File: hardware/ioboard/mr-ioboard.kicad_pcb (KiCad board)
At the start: 4 copper layers, 65 x 80 mm, 126 parts, among them J1 Conn_01x40_Shielded, J2 USB_C_Receptacle_USB2.0, J3 Conn_01x06, J4 Micro_SD_Card_Det, J5 Conn_01x04, J6 Conn_01x02, Q1 2N7002, SW1 SW_Push, U1 TPS62822, U10 F1C200S, U11 TPS54202DDC, U2 TPS56637, U3 TPD2E2U06, U4 DS90C363, U5 TPD2E2U06, U6 LD3985M28R_SOT23, U7 TPS62822, U8 FUSB302BMPX, U9 TPD2E2U06, Y1 24MHz

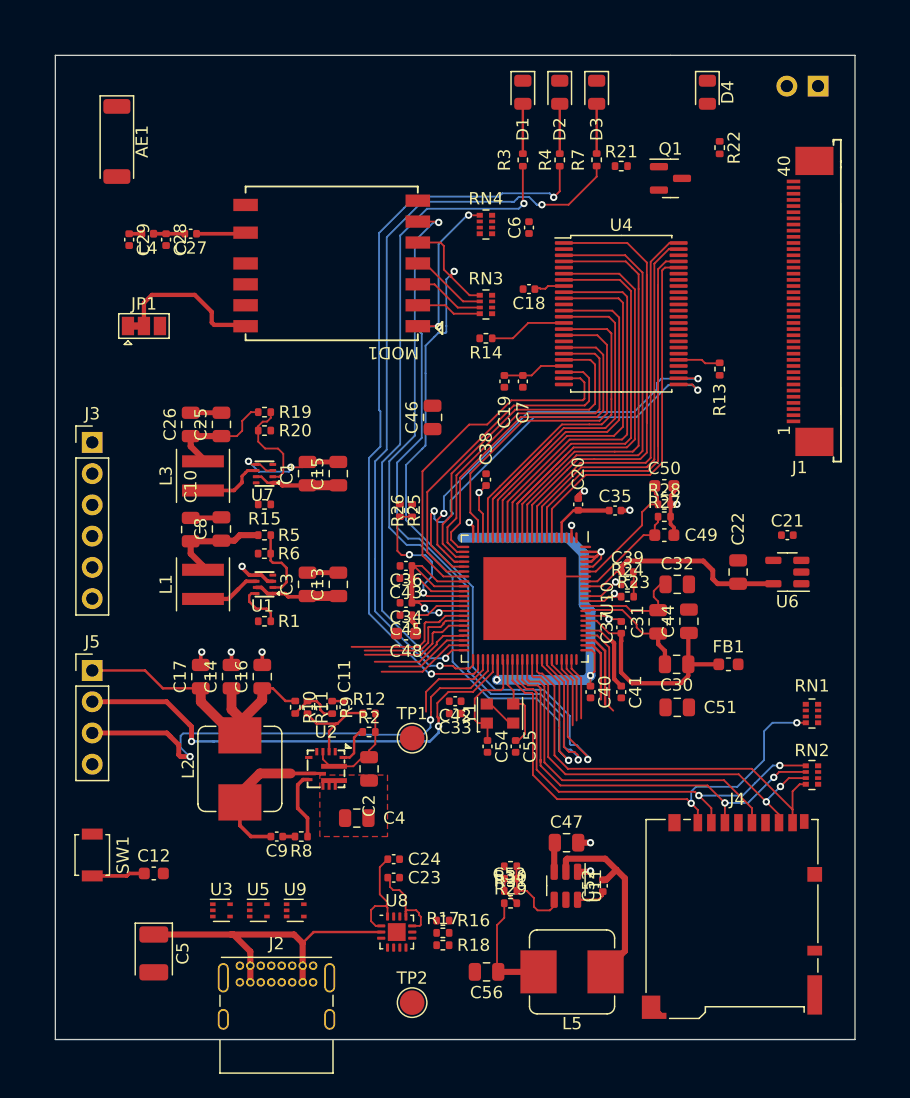
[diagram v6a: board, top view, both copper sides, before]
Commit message: First pass at routing IO board
Signed-off-by: gatecat <gatecat@ds0.me>
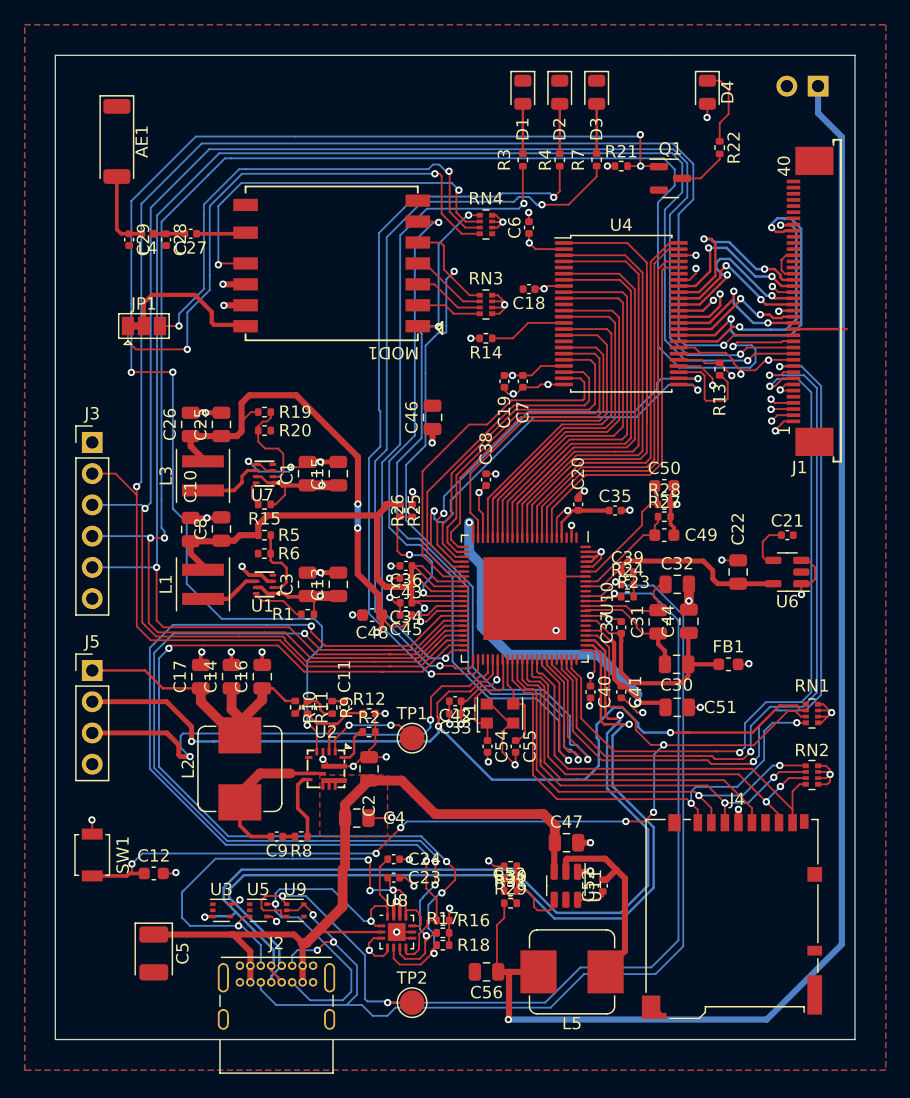
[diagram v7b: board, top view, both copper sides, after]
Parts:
- moved R1 3.55 mm to (120.5, 95.4), turned to 180 degrees
- moved C48 3.13 mm to (125.8, 95.5)
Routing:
- net /FPGA_JTAG_TCK: track 0.00 -> 143.0 mm, vias 0 -> 3
- net /FPGA_JTAG_TMS: track 6.94 -> 140.1 mm, vias 0 -> 2
- net /FPGA_JTAG_TDI: track 8.23 -> 138.8 mm, vias 0 -> 2
- net /FPGA_JTAG_TDO: track 9.51 -> 137.3 mm, vias 0 -> 2
- net /3V3_PG: track 0.00 -> 107.3 mm, vias 0 -> 5
- net /VLED: track 9.14 -> 113.2 mm, vias 0 -> 1
- net /SBU: track 3.59 -> 91.9 mm, vias 1 -> 4
- net /TVIN1: track 3.31 -> 83.2 mm, vias 1 -> 3
- net GND: track 59.3 -> 138.4 mm, vias 14 -> 57
- net +1V1: track 23.2 -> 96.6 mm, vias 1 -> 5
- net /USB_INT: track 7.57 -> 77.2 mm, vias 0 -> 4
- net /RESET: track 11.9 -> 81.3 mm, vias 0 -> 6
- net /USB_D+: track 6.31 -> 75.1 mm, vias 0 -> 2
- net /USB_D-: track 5.24 -> 73.6 mm, vias 0 -> 2
- net /I2C_SCL: track 9.84 -> 75.9 mm, vias 0 -> 4
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- added copper zone on In2.Cu, net +3V3
- added copper zone on B.Cu, net GND
- added copper zone on F.Cu, net GND
- added copper zone on In1.Cu, net GND

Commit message: Tidy up IO board silk
Signed-off-by: gatecat <gatecat@ds0.me>
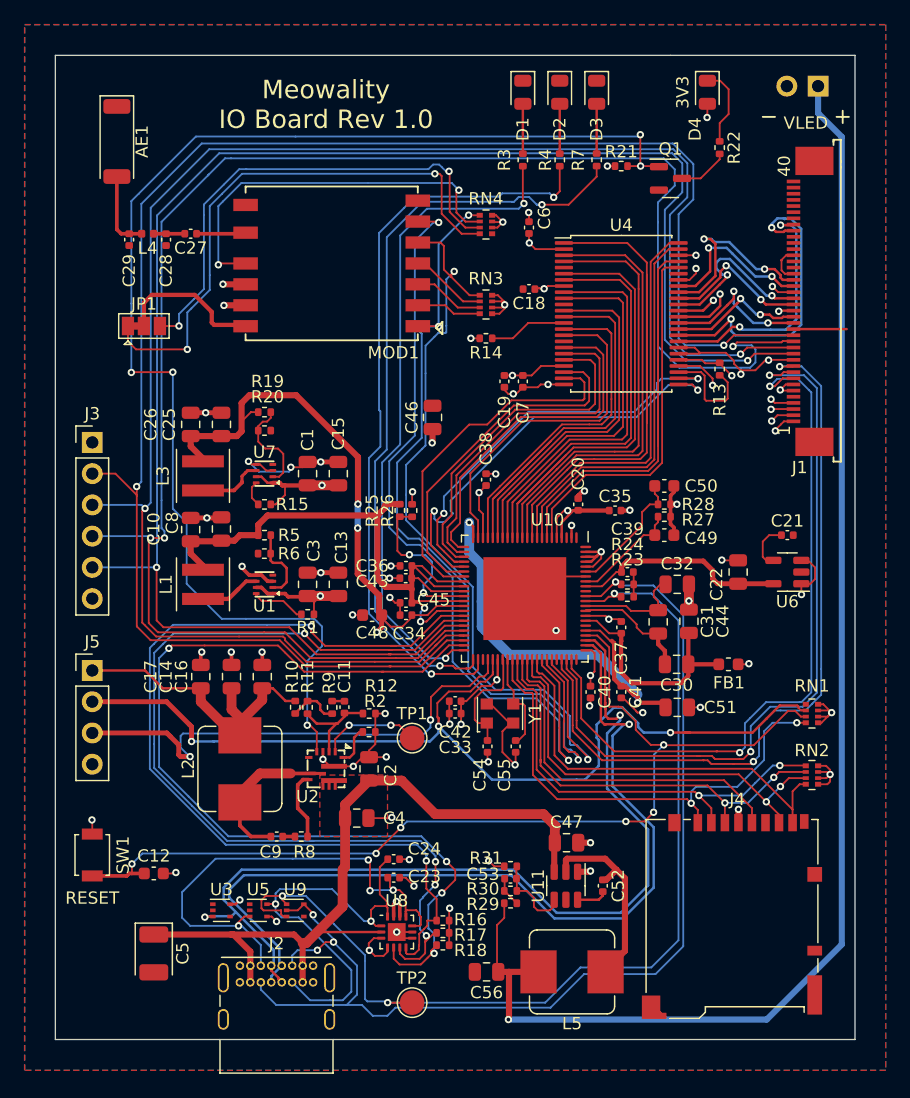
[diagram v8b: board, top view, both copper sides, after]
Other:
- board text added: "3V3"
- board text added: "GND"
- board text added: "Meowality IO Board Rev 1.0"
- board text added: "RESET"
- board text added: "RX"
- board text added: "TCK"
- board text added: "TDI"
- board text added: "TDO"
- board text added: "TMS"
- board text added: "TX"
- board text added: "VLED"
